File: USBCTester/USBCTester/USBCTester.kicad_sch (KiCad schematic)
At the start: 81 parts, among them J1 AUSB1-DFN-PTR3, J2 AUSB1-DFN-PTR3, J3 Conn_01x12, J4 Conn_01x03, J6 Conn_01x03, SW1 SW_Push, U1 74HC595, U2 74HC595, U3 74HC595, U4 74HC595, U5 74HC595, U6 74HC595, U7 RaspberryPi_Pico

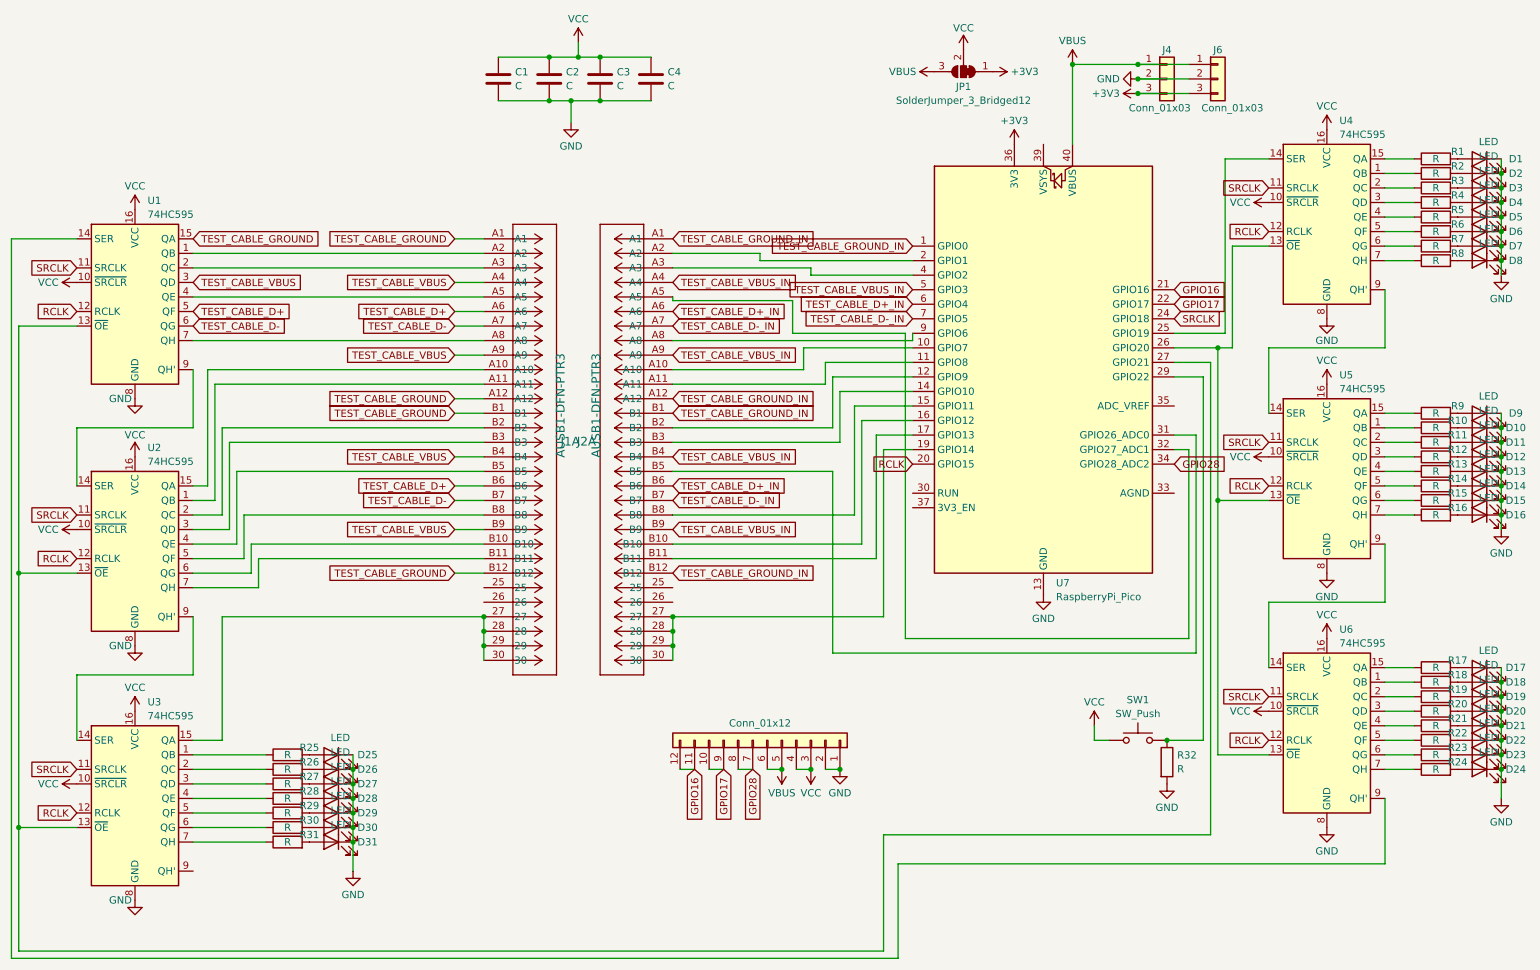
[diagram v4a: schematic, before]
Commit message: add 3rd incompatible footprint design
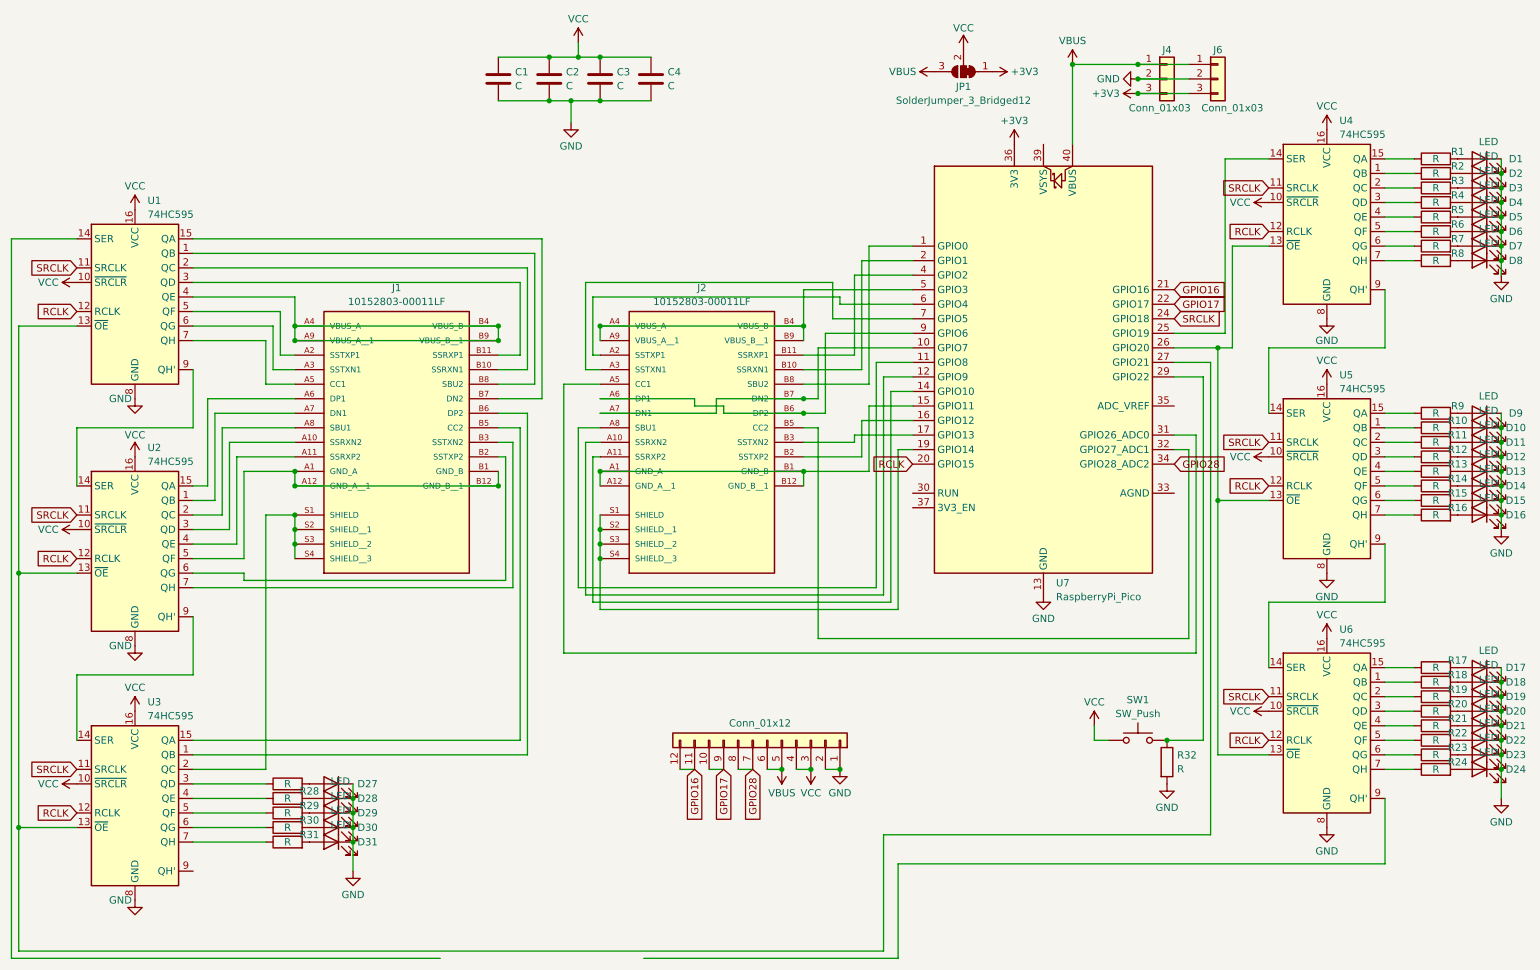
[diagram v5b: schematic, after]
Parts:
- removed D25, D26: LED, LED_SMD:LED_0603_1608Metric, symbol Device:LED
- removed J1, J2: AUSB1-DFN-PTR3, USBCFootprint:USBCConnector_WithShield, symbol USBCSymbol:AUSB1-DFN-PTR3
- removed R25, R26: R, Resistor_SMD:R_0603_1608Metric, symbol Device:R
- added J1, J2: 10152803-00011LF, USBCFootprint:AMPHENOL_10152803-00011LF, symbol USBCSymbol:10152803-00011LF
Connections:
- net at U1.1 (QB): now also J1.B8 (SBU2)
- net at U1.14 (SER): no longer U6.9 (QH')
- net at U1.2 (QC): now also J1.B10 (SSRXN1)
- net at U1.4 (QE): now also J1.A4 (VBUS_A), J1.A9 (VBUS_A__1), J1.B4 (VBUS_B), J1.B9 (VBUS_B__1)
- net at U1.7 (QH): now also J1.A5 (CC1)
- net at U7.10 (GPIO7): now also J2.A7 (DN1), J2.B7 (DN2)
- net at U7.11 (GPIO8): now also J2.A8 (SBU1)
- net at U7.12 (GPIO9): now also J2.A10 (SSRXN2)
- net at U7.14 (GPIO10): now also J2.A11 (SSRXP2)
- net at U7.15 (GPIO11): now also J2.A1 (GND_A), J2.A12 (GND_A__1), J2.B1 (GND_B), J2.B12 (GND_B__1)
- net at U7.16 (GPIO12): now also J2.B2 (SSTXP2)
- net at U7.17 (GPIO13): now also J2.B3 (SSTXN2)
- net at U7.19 (GPIO14): now also J2.S1 (SHIELD), J2.S2 (SHIELD__1), J2.S3 (SHIELD__2), J2.S4 (SHIELD__3)
- net at U7.2 (GPIO1): now also J2.B10 (SSRXN1)
- net at U7.31 (GPIO26_ADC0): now also J2.A5 (CC1)
- net at U7.32 (GPIO27_ADC1): now also J2.B5 (CC2)
- net at U7.4 (GPIO2): now also J2.B11 (SSRXP1)
- net at U7.9 (GPIO6): now also J2.A6 (DP1), J2.B6 (DP2)
- net at U3.2 (QC): now also J1.S1 (SHIELD), J1.S2 (SHIELD__1), J1.S3 (SHIELD__2), J1.S4 (SHIELD__3)
- net at U2.1 (QB): now also J1.A7 (DN1)
- net at U2.15 (QA): now also J1.A6 (DP1)
- net at U2.2 (QC): now also J1.A8 (SBU1)
- net at U2.3 (QD): now also J1.A10 (SSRXN2)
- net at U2.4 (QE): now also J1.A11 (SSRXP2)
- net at U2.5 (QF): now also J1.A1 (GND_A), J1.A12 (GND_A__1), J1.B1 (GND_B), J1.B12 (GND_B__1)
- net at U2.6 (QG): now also J1.B2 (SSTXP2)
- net at U2.7 (QH): now also J1.B3 (SSTXN2)
- net at U3.15 (QA): now also J1.B5 (CC2)
- net at U3.1 (QB): now also J1.B6 (DP2)
- net TEST_CABLE_D+: no longer names the net of U1.5 (QF)
- net TEST_CABLE_D+: now also J1.A2 (SSTXP1)
- net TEST_CABLE_D+_IN: no longer names the net of U7.6 (GPIO4)
- net TEST_CABLE_D+_IN: now also J2.A2 (SSTXP1)
- net TEST_CABLE_D-: no longer names the net of U1.6 (QG)
- net TEST_CABLE_D-: now also J1.A3 (SSTXN1)
- net TEST_CABLE_D-_IN: no longer names the net of U7.7 (GPIO5)
- net TEST_CABLE_D-_IN: now also J2.A3 (SSTXN1)
- net TEST_CABLE_GROUND: no longer names the net of U1.15 (QA)
- net TEST_CABLE_GROUND: now also J1.B7 (DN2)
- net TEST_CABLE_GROUND_IN: no longer names the net of U7.1 (GPIO0)
- net TEST_CABLE_GROUND_IN: now also J2.B8 (SBU2)
- net TEST_CABLE_VBUS: no longer names the net of U1.3 (QD)
- net TEST_CABLE_VBUS: now also J1.B11 (SSRXP1)
- net TEST_CABLE_VBUS_IN: no longer names the net of U7.5 (GPIO3)
- net TEST_CABLE_VBUS_IN: now also J2.A4 (VBUS_A), J2.A9 (VBUS_A__1), J2.B4 (VBUS_B), J2.B9 (VBUS_B__1)

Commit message: switch to USB4080 footprint
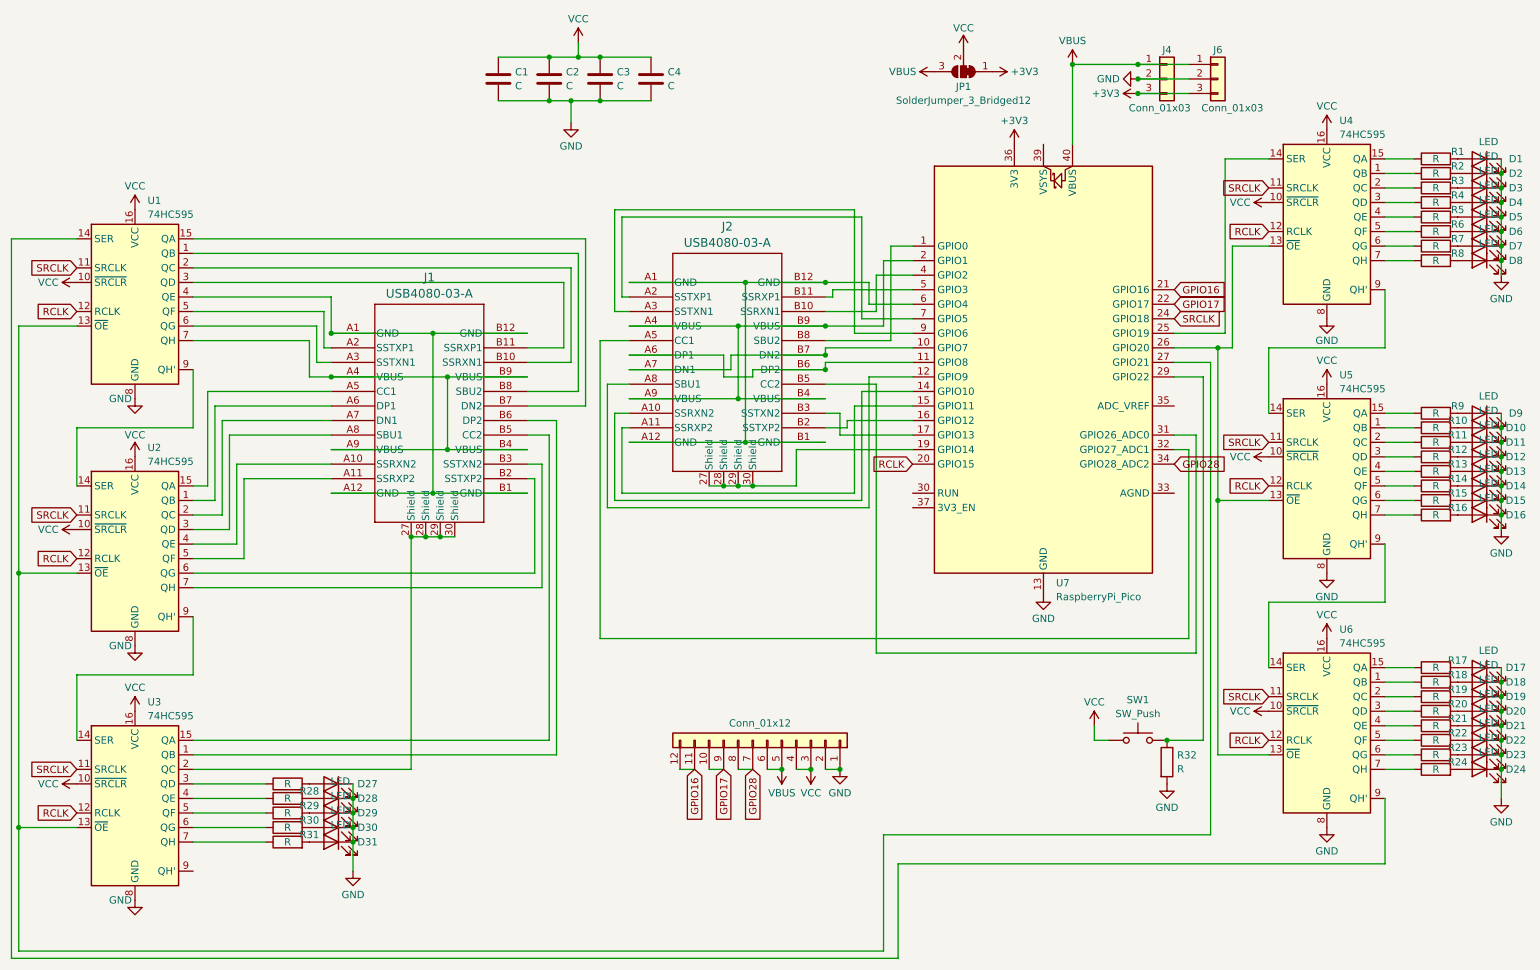
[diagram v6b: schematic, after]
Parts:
- removed J1, J2: 10152803-00011LF, USBCFootprint:AMPHENOL_10152803-00011LF, symbol USBCSymbol:10152803-00011LF
- added J1, J2: USB4080-03-A, USB4080-03-A_GCT, symbol USBCSymbol:USB4080-03-A
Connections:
- net at U1.1 (QB): now also J1.B8 (SBU2)
- net at U1.14 (SER): now also U6.9 (QH')
- net at U1.15 (QA): now also J1.B7 (DN2)
- net at U1.2 (QC): now also J1.B10 (SSRXN1)
- net at U1.3 (QD): now also J1.B11 (SSRXP1)
- net at U1.4 (QE): now also J1.A1 (GND), J1.A12 (GND), J1.B1 (GND), J1.B12 (GND)
- net at U1.5 (QF): now also J1.A2 (SSTXP1)
- net at U1.6 (QG): now also J1.A3 (SSTXN1)
- net at U1.7 (QH): now also J1.A4 (VBUS), J1.A9 (VBUS), J1.B4 (VBUS), J1.B9 (VBUS)
- net at U7.1 (GPIO0): now also J2.B8 (SBU2)
- net at U7.10 (GPIO7): now also J2.A7 (DN1), J2.B7 (DN2)
- net at U7.11 (GPIO8): now also J2.A6 (DP1), J2.B6 (DP2)
- net at U7.12 (GPIO9): now also J2.A8 (SBU1)
- net at U7.14 (GPIO10): now also J2.A10 (SSRXN2)
- net at U7.15 (GPIO11): now also J2.A11 (SSRXP2)
- net at U7.16 (GPIO12): now also J2.B2 (SSTXP2)
- net at U7.17 (GPIO13): now also J2.B3 (SSTXN2)
- net at U7.19 (GPIO14): now also J2.27 (Shield), J2.28 (Shield), J2.29 (Shield), J2.30 (Shield)
- net at U7.2 (GPIO1): now also J2.A4 (VBUS), J2.A9 (VBUS), J2.B4 (VBUS), J2.B9 (VBUS)
- net at U7.31 (GPIO26_ADC0): now also J2.B5 (CC2)
- net at U7.32 (GPIO27_ADC1): now also J2.A5 (CC1)
- net at U7.4 (GPIO2): now also J2.B10 (SSRXN1)
- net at U7.5 (GPIO3): now also J2.B11 (SSRXP1)
- net at U7.6 (GPIO4): now also J2.A1 (GND), J2.A12 (GND), J2.B1 (GND), J2.B12 (GND)
- net at U7.7 (GPIO5): now also J2.A2 (SSTXP1)
- net at U7.9 (GPIO6): now also J2.A3 (SSTXN1)
- net at U2.1 (QB): now also J1.A6 (DP1)
- net at U2.15 (QA): now also J1.A5 (CC1)
- net at U2.2 (QC): now also J1.A7 (DN1)
- net at U2.3 (QD): now also J1.A8 (SBU1)
- net at U2.4 (QE): now also J1.A10 (SSRXN2)
- net at U2.5 (QF): now also J1.A11 (SSRXP2)
- net at U2.6 (QG): now also J1.B2 (SSTXP2)
- net at U2.7 (QH): now also J1.B3 (SSTXN2)
- net at U3.15 (QA): now also J1.B5 (CC2)
- net at U3.1 (QB): now also J1.B6 (DP2)
- net at U3.2 (QC): now also J1.27 (Shield), J1.28 (Shield), J1.29 (Shield), J1.30 (Shield)

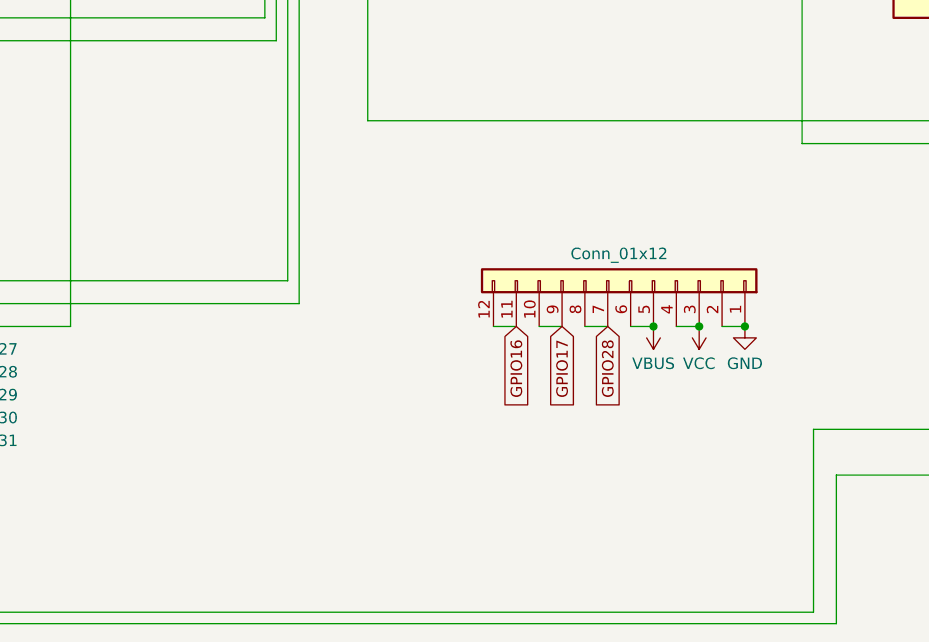
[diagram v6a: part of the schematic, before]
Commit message: add protoboard, lots of tweaks and silkscreen improvements
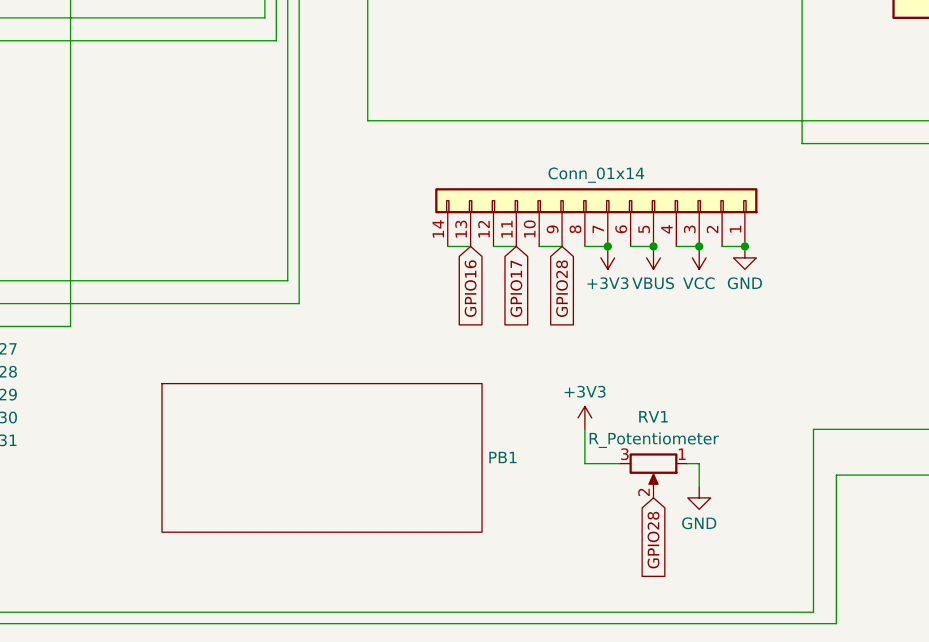
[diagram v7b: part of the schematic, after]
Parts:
- added PB1: ~, ProtoBoard:ProtoBoard 14x6, symbol ProtoBoard:14x6ProtoBoard
- added RV1: R_Potentiometer, Potentiometer_SMD:Potentiometer_Vishay_TS53YL_Vertical, symbol Device:R_Potentiometer
- J1, J2: footprint USB4080-03-A_GCT -> USBCFootprint:USB4080-03-A_GCT_RoundHoles
- J3: value Conn_01x12 -> Conn_01x14; footprint Connector_PinSocket_2.54mm:PinSocket_1x12_P2.54mm_Vertical -> Connector_PinSocket_2.54mm:PinSocket_1x14_P2.54mm_Vertical; symbol Connector_Generic:Conn_01x12 -> Connector_Generic:Conn_01x14
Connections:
- net +3V3: now also J3.7 (Pin_7), J3.8 (Pin_8), RV1.3
- net GND: now also RV1.1
- net GPIO16: now also J3.13 (Pin_13), J3.14 (Pin_14); no longer J3.11 (Pin_11), J3.12 (Pin_12)
- net GPIO17: now also J3.11 (Pin_11), J3.12 (Pin_12); no longer J3.10 (Pin_10), J3.9 (Pin_9)
- net GPIO28: now also J3.10 (Pin_10), J3.9 (Pin_9), RV1.2; no longer J3.7 (Pin_7), J3.8 (Pin_8)
